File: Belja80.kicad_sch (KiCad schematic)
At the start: 223 parts, among them J1 USB_C_Receptacle_USB2.0, SW1 SW_Esc, SW10 SW_F9, SW11 SW_F10, SW12 SW_F11, SW13 SW_F12, SW14 SW_PrintSc, SW15 SW_ScrollLock, SW16 SW_§, SW17 SW_1, SW18 SW_2, SW19 SW_3, SW2 SW_F1, SW20 SW_4, SW21 SW_6, SW22 SW_7, SW23 SW_8, SW24 SW_0, SW25 SW_+, SW26 SW_|, SW27 SW_Backspace, SW28 SW_Insert, SW29 SW_Home, SW3 SW_F2, SW30 SW_Pause, SW31 SW_Tab, SW32 SW_Q, SW33 SW_W, SW34 SW_E, SW35 SW_R, SW36 SW_5, SW37 SW_Y, SW38 SW_9, SW39 SW_O, SW4 SW_F3, SW40 SW_P, SW41 SW_Å, SW42 SW_^, SW43 SW_Delete, SW44 SW_End, SW45 SW_PgUp, SW46 SW_Caps, SW47 SW_A, SW48 SW_S, SW49 SW_D, SW5 SW_F4, SW50 SW_F, SW51 SW_T, SW52 SW_U, SW53 SW_I, SW54 SW_L, SW55 SW_Æ, SW56 SW_Ø, SW57 SW_*, SW58 SW_\, SW59 SW_ArrowUp, SW6 SW_F5, SW60 SW_PgDn, SW61 SW_LShift2.25u, SW62 SW_EnterISO, SW63 SW_LShift1.25u, SW64 SW_<>, SW65 SW_Z, SW66 SW_X, SW67 SW_C, SW68 SW_G, SW69 SW_H, SW7 SW_F6, SW70 SW_J, SW71 SW_K, SW72 SW_dot, SW73 SW_-, SW74 SW_RShift2.75u, SW75 SW_EnterANSI, SW76 SW_ArrowDown, SW77 SW_ArrowRight, SW78 SW_Ctrl, SW79 SW_Win, SW8 SW_F7, SW80 SW_Alt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

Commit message: update
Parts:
- R5: footprint Resistor_SMD:R_0402_1005Metric -> Resistor_SMD:R_0603_1608Metric
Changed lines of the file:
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@@
       (effects (font (size 1.27 1.27)) (justify left))
     )
-    (property "Footprint" "Resistor_SMD:R_0402_1005Metric" (at 284.48 203.2 0)
+    (property "Footprint" "Resistor_SMD:R_0603_1608Metric" (at 284.48 203.2 0)
       (effects (font (size 1.27 1.27)) hide)
     )

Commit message: Component layout
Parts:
- added H9: M3, MountingHole:MountingHole_3.2mm_M3_ISO7380_Pad, symbol Mechanical:MountingHole_Pad
- H1, H2, H3, H4, H5, H6, H7, H8: footprint MountingHole:MountingHole_3.2mm_M3_Pad_Via -> MountingHole:MountingHole_3.2mm_M3_ISO7380_Pad
- J1: footprint Connector_USB:USB_C_Receptacle_Palconn_UTC16-G -> Belja80:USB_C_Receptacle_Palconn_UTC16-G
- R1, R2, R8: footprint Resistor_SMD:R_0603_1608Metric -> Resistor_SMD:R_0402_1005Metric
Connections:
- net +3V3: no longer U1.26 (RUN)
- net GND: now also H9.1
- net ~{RESET}: now reaches C16.1, R9.1, SW93.2, SW93.4
- net ~{RESET}: now also U1.26 (RUN)
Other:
- moved on the sheet: C16, R9, SW93

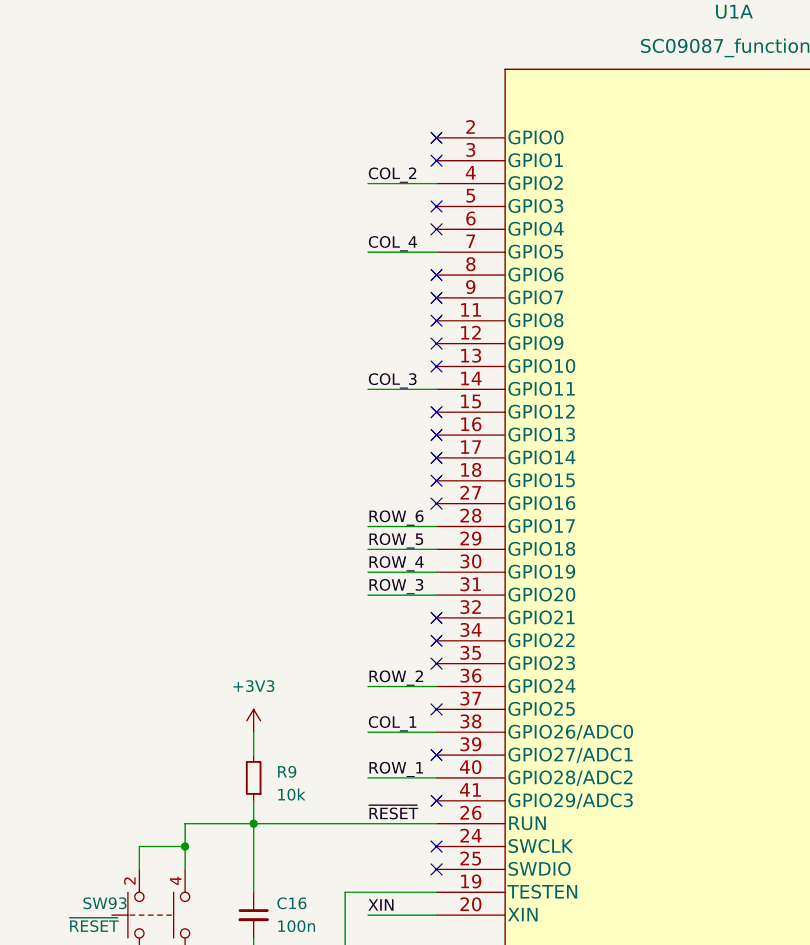
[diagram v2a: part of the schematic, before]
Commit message: routing µC section and silkscreen
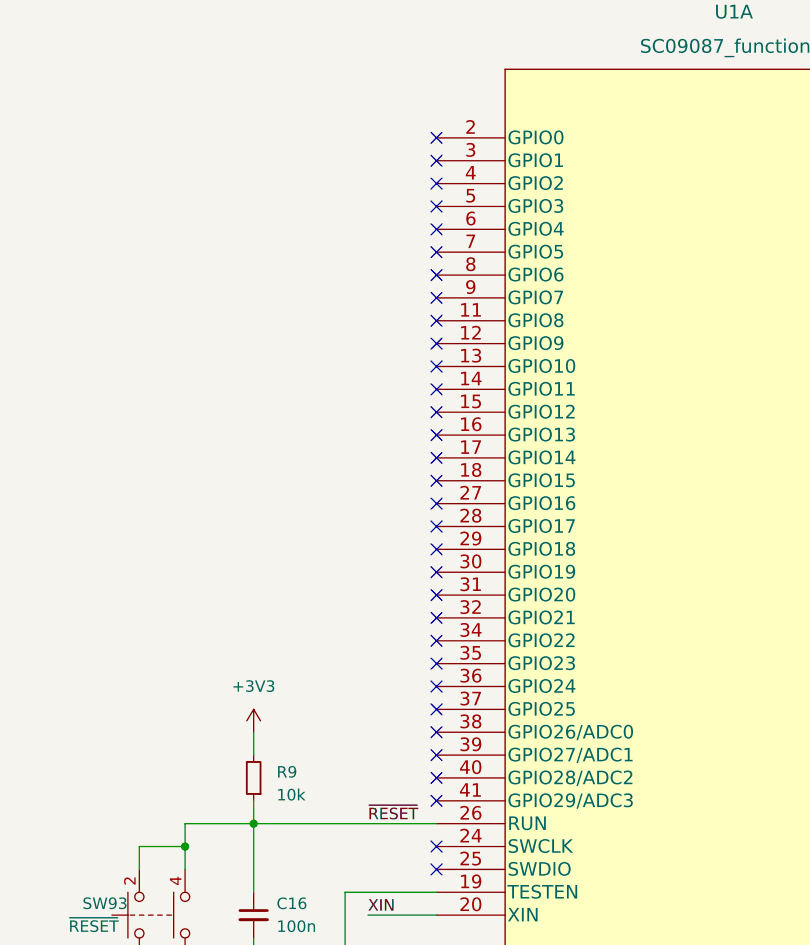
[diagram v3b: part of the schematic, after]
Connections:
- net COL_1: no longer U1.38 (GPIO26/ADC0)
- net COL_2: no longer U1.4 (GPIO2)
- net COL_3: no longer U1.14 (GPIO11)
- net COL_4: no longer U1.7 (GPIO5)
- net ROW_1: no longer U1.40 (GPIO28/ADC2)
- net ROW_2: no longer U1.36 (GPIO24)
- net ROW_3: no longer U1.31 (GPIO20)
- net ROW_4: no longer U1.30 (GPIO19)
- net ROW_5: no longer U1.29 (GPIO18)
- net ROW_6: no longer U1.28 (GPIO17)
- no-connect marks 25 -> 35
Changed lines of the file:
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@@
   (no_connect (at 76.2 195.58))
   (no_connect (at 76.2 203.2))
+  (no_connect (at 76.2 190.5))
+  (no_connect (at 76.2 220.98))
   (no_connect (at 76.2 213.36))
   (no_connect (at 76.2 200.66))
@@
   (no_connect (at 76.2 251.46))
   (no_connect (at 76.2 180.34))
+  (no_connect (at 76.2 223.52))
   (no_connect (at 76.2 177.8))
   (no_connect (at 76.2 246.38))
   (no_connect (at 76.2 208.28))
+  (no_connect (at 76.2 238.76))
   (no_connect (at 76.2 210.82))
   (no_connect (at 76.2 187.96))
@@
   (no_connect (at 76.2 259.08))
   (no_connect (at 76.2 256.54))
+  (no_connect (at 76.2 248.92))
   (no_connect (at 251.46 210.82))
   (no_connect (at 76.2 198.12))
   (no_connect (at 228.6 218.44))
+  (no_connect (at 76.2 243.84))
   (no_connect (at 251.46 208.28))
+  (no_connect (at 76.2 205.74))
+  (no_connect (at 76.2 228.6))
+  (no_connect (at 76.2 226.06))
   (no_connect (at 76.2 185.42))
+  (no_connect (at 76.2 182.88))
   (no_connect (at 76.2 236.22))
   (no_connect (at 76.2 233.68))
@@
     (stroke (width 0) (type default))
   )
-  (wire (pts (xy 68.58 243.84) (xy 76.2 243.84))
-    (stroke (width 0) (type default))
-  )
   (wire (pts (xy 218.44 134.62) (xy 226.06 134.62))
     (stroke (width 0) (type default))
@@
     (stroke (width 0) (type default))
   )
-  (wire (pts (xy 68.58 238.76) (xy 76.2 238.76))
-    (stroke (width 0) (type default))
-  )
   (wire (pts (xy 314.96 180.34) (xy 314.96 193.04))
     (stroke (width 0) (type default))
@@
     (stroke (width 0) (type default))
   )
-  (wire (pts (xy 68.58 190.5) (xy 76.2 190.5))
-    (stroke (width 0) (type default))
-  )
   (wire (pts (xy 358.14 101.6) (xy 358.14 104.14))
     (stroke (width 0) (type default))
@@
     (stroke (width 0) (type default))
   )
-  (wire (pts (xy 68.58 182.88) (xy 76.2 182.88))
-    (stroke (width 0) (type default))
-  )
   (wire (pts (xy 218.44 53.34) (xy 226.06 53.34))
     (stroke (width 0) (type default))
@@
     (stroke (width 0) (type default))
   )
-  (wire (pts (xy 68.58 226.06) (xy 76.2 226.06))
-    (stroke (width 0) (type default))
-  )
   (wire (pts (xy 180.34 198.12) (xy 182.88 198.12))
     (stroke (width 0) (type default))
@@
     (stroke (width 0) (type default))
   )
-  (wire (pts (xy 68.58 223.52) (xy 76.2 223.52))
-    (stroke (width 0) (type default))
-  )
   (wire (pts (xy 256.54 177.8) (xy 256.54 180.34))
     (stroke (width 0) (type default))
@@
     (stroke (width 0) (type default))
   )
-  (wire (pts (xy 68.58 228.6) (xy 76.2 228.6))
-    (stroke (width 0) (type default))
-  )
   (wire (pts (xy 256.54 104.14) (xy 281.94 104.14))
     (stroke (width 0) (type default))
@@
     (stroke (width 0) (type default))
   )
-  (wire (pts (xy 68.58 248.92) (xy 76.2 248.92))
-    (stroke (width 0) (type default))
-  )
   (wire (pts (xy 304.8 210.82) (xy 314.96 210.82))
     (stroke (width 0) (type default))
@@
     (stroke (width 0) (type default))
   )
-  (wire (pts (xy 68.58 220.98) (xy 76.2 220.98))
-    (stroke (width 0) (type default))
-  )
   (wire (pts (xy 40.64 53.34) (xy 48.26 53.34))
     (stroke (width 0) (type default))
@@
   )
   (wire (pts (xy 264.16 248.92) (xy 264.16 254))
-    (stroke (width 0) (type default))
-  )
-  (wire (pts (xy 68.58 205.74) (xy 76.2 205.74))
     (stroke (width 0) (type default))
   )
@@
     (effects (font (size 1.27 1.27)) (justify left bottom))
   )
-  (label "ROW_4" (at 68.58 226.06 0) (fields_autoplaced)
-    (effects (font (size 1.27 1.27)) (justify left bottom))
-  )
   (label "ROW_2" (at 15.24 63.5 0) (fields_autoplaced)
     (effects (font (size 1.27 1.27)) (justify left bottom))
   )
-  (label "COL_4" (at 68.58 190.5 0) (fields_autoplaced)
-    (effects (font (size 1.27 1.27)) (justify left bottom))
-  )
-  (label "ROW_5" (at 68.58 223.52 0) (fields_autoplaced)
-    (effects (font (size 1.27 1.27)) (justify left bottom))
-  )
   (label "USB_D-" (at 261.62 195.58 180) (fields_autoplaced)
     (effects (font (size 1.27 1.27)) (justify right bottom))
@@
     (effects (font (size 1.27 1.27)) (justify right bottom))
   )
-  (label "ROW_3" (at 68.58 228.6 0) (fields_autoplaced)
-    (effects (font (size 1.27 1.27)) (justify left bottom))
-  )
   (label "COL_5" (at 149.86 15.24 270) (fields_autoplaced)
     (effects (font (size 1.27 1.27)) (justify right bottom))
-  )
-  (label "ROW_6" (at 68.58 220.98 0) (fields_autoplaced)
-    (effects (font (size 1.27 1.27)) (justify left bottom))
   )
   (label "COL_7" (at 200.66 15.24 270) (fields_autoplaced)
@@
     (effects (font (size 1.27 1.27)) (justify left bottom))
   )
-  (label "ROW_2" (at 68.58 238.76 0) (fields_autoplaced)
-    (effects (font (size 1.27 1.27)) (justify left bottom))
-  )
   (label "XOUT" (at 154.94 177.8 180) (fields_autoplaced)
     (effects (font (size 1.27 1.27)) (justify right bottom))
@@
     (effects (font (size 1.27 1.27)) (justify right bottom))
   )
-  (label "ROW_1" (at 68.58 248.92 0) (fields_autoplaced)
-    (effects (font (size 1.27 1.27)) (justify left bottom))
-  )
   (label "COL_10" (at 276.86 15.24 270) (fields_autoplaced)
     (effects (font (size 1.27 1.27)) (justify right bottom))
@@
     (effects (font (size 1.27 1.27)) (justify right bottom))
   )
-  (label "COL_1" (at 68.58 243.84 0) (fields_autoplaced)
-    (effects (font (size 1.27 1.27)) (justify left bottom))
-  )
   (label "QSPI_SD0" (at 259.08 264.16 180) (fields_autoplaced)
     (effects (font (size 1.27 1.27)) (justify right bottom))
@@
     (effects (font (size 1.27 1.27)) (justify right bottom))
   )
-  (label "COL_3" (at 68.58 205.74 0) (fields_autoplaced)
-    (effects (font (size 1.27 1.27)) (justify left bottom))
-  )
   (label "QSPI_SD2" (at 213.36 259.08 0) (fields_autoplaced)
     (effects (font (size 1.27 1.27)) (justify left bottom))
@@
     (effects (font (size 1.27 1.27)) (justify right bottom))
   )
-  (label "COL_2" (at 68.58 182.88 0) (fields_autoplaced)
-    (effects (font (size 1.27 1.27)) (justify left bottom))
-  )
   (label "ROW_5" (at 15.24 124.46 0) (fields_autoplaced)

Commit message: Routing
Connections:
- net COL_1: now also U1.27 (GPIO16)
- net COL_10: now also U1.2 (GPIO0)
- net COL_11: now also U1.4 (GPIO2)
- net COL_12: now also U1.5 (GPIO3)
- net COL_13: now also U1.11 (GPIO8)
- net COL_14: now also U1.12 (GPIO9)
- net COL_15: now also U1.13 (GPIO10)
- net COL_2: now also U1.28 (GPIO17)
- net COL_3: now also U1.30 (GPIO19)
- net COL_4: now also U1.31 (GPIO20)
- net COL_5: now also U1.32 (GPIO21)
- net COL_6: now also U1.29 (GPIO18)
- net COL_7: now also U1.35 (GPIO23)
- net COL_8: now also U1.37 (GPIO25)
- net COL_9: now also U1.39 (GPIO27/ADC1)
- net ROW_1: now also U1.3 (GPIO1)
- net ROW_2: now also U1.14 (GPIO11)
- net ROW_3: now also U1.15 (GPIO12)
- net ROW_4: now also U1.16 (GPIO13)
- net ROW_5: now also U1.17 (GPIO14)
- net ROW_6: now also U1.18 (GPIO15)
- no-connect marks 35 -> 14

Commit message: Stepped Caps Lock support
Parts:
- added SW94: SW_CapsStep, Belja80:SW_Cherry_MX_1.25u_PCB, symbol Switch:SW_Push
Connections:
- net COL_1: now also SW94.2
- net at D46.2 (A), SW46.1: now also SW94.1
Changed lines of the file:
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@@
   (junction (at 53.34 43.18) (diameter 0) (color 0 0 0 0)
   )
+  (junction (at 27.94 93.98) (diameter 0) (color 0 0 0 0)
+  )
   (junction (at 378.46 53.34) (diameter 0) (color 0 0 0 0)
   )
@@
   (junction (at 104.14 124.46) (diameter 0) (color 0 0 0 0)
   )
+  (junction (at 48.26 88.9) (diameter 0) (color 0 0 0 0)
+  )
   (junction (at 281.94 144.78) (diameter 0) (color 0 0 0 0)
   )
@@
     (stroke (width 0) (type default))
   )
+  (wire (pts (xy 30.48 88.9) (xy 27.94 88.9))
+    (stroke (width 0) (type default))
+  )
   (wire (pts (xy 307.34 144.78) (xy 332.74 144.78))
     (stroke (width 0) (type default))
@@
     (stroke (width 0) (type default))
   )
+  (wire (pts (xy 48.26 88.9) (xy 48.26 93.98))
+    (stroke (width 0) (type default))
+  )
   (wire (pts (xy 27.94 109.22) (xy 27.94 114.3))
     (stroke (width 0) (type default))
@@
     (stroke (width 0) (type default))
   )
+  (wire (pts (xy 40.64 88.9) (xy 48.26 88.9))
+    (stroke (width 0) (type default))
+  )
   (wire (pts (xy 218.44 93.98) (xy 226.06 93.98))
     (stroke (width 0) (type default))
@@
     (stroke (width 0) (type default))
   )
+  (wire (pts (xy 27.94 88.9) (xy 27.94 93.98))
+    (stroke (width 0) (type default))
+  )
   (wire (pts (xy 165.1 185.42) (xy 165.1 187.96))
     (stroke (width 0) (type default))
@@
     (stroke (width 0) (type default))
   )
-  (wire (pts (xy 48.26 73.66) (xy 48.26 93.98))
+  (wire (pts (xy 48.26 73.66) (xy 48.26 88.9))
     (stroke (width 0) (type default))
   )
@@
   )
   (symbol (lib_id "Switch:SW_Push") (at 35.56 93.98 0) (unit 1)
-    (in_bom yes) (on_board yes) (dnp no) (fields_autoplaced)
-    (property "Reference" "SW46" (at 35.56 86.36 0)
+    (in_bom yes) (on_board yes) (dnp no)
+    (property "Reference" "SW46" (at 30.48 91.44 0)
       (effects (font (size 1.27 1.27)))
     )
-    (property "Value" "SW_Caps" (at 35.56 88.9 0)
+    (property "Value" "SW_Caps" (at 40.64 91.44 0)
       (effects (font (size 1.27 1.27)))
     )
@@
         )
       )
+    )
+  )
+  (symbol (lib_id "Switch:SW_Push") (at 35.56 88.9 0) (unit 1)
+    (in_bom yes) (on_board yes) (dnp no)
+    (property "Reference" "SW94" (at 30.48 86.36 0)
+      (effects (font (size 1.27 1.27)))
+    )
+    (property "Value" "SW_CapsStep" (at 41.91 86.36 0)
+      (effects (font (size 1.27 1.27)))
+    )
+    (property "Footprint" "Belja80:SW_Cherry_MX_1.25u_PCB" (at 35.56 83.82 0)
+      (effects (font (size 1.27 1.27)) hide)
+    )
+    (property "Datasheet" "~" (at 35.56 83.82 0)
+      (effects (font (size 1.27 1.27)) hide)
+    )
+    (pin "1")
+    (pin "2")
+    (instances
+      (project "Belja80"
+        (path "/e63e39d7-6ac0-4ffd-8aa3-1841a4541b55"
+          (reference "SW94") (unit 1)
+        )
+      )

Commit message: Ready for production
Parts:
- FB1: value 600R@100MHz -> 220R@100MHz
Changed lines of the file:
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@@
   (symbol (lib_id "Device:FerriteBead_Small") (at 276.86 180.34 90) (unit 1)
     (in_bom yes) (on_board yes) (dnp no) (fields_autoplaced)
-    (property "Reference" "FB1" (at 276.8219 173.99 90)
+    (property "Reference" "FB1" (at 276.8219 175.26 90)
       (effects (font (size 1.27 1.27)))
     )
-    (property "Value" "600R@100MHz" (at 276.8219 176.53 90)
+    (property "Value" "220R@100MHz" (at 276.8219 177.8 90)
       (effects (font (size 1.27 1.27)))
     )
